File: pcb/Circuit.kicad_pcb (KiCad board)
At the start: 2 copper layers, 82.4 x 68.9 mm, 51 parts, among them J1 DTM13-12PA-R008, J2 TSW-101-07-T-D, J3 TSW-101-07-T-D, U1 MCP1700-1802E_TO92, U2 CDP68HC68S1, U3 LM2672N-5.0, U4 Teensy4.0, U5 MCP2562-H-P

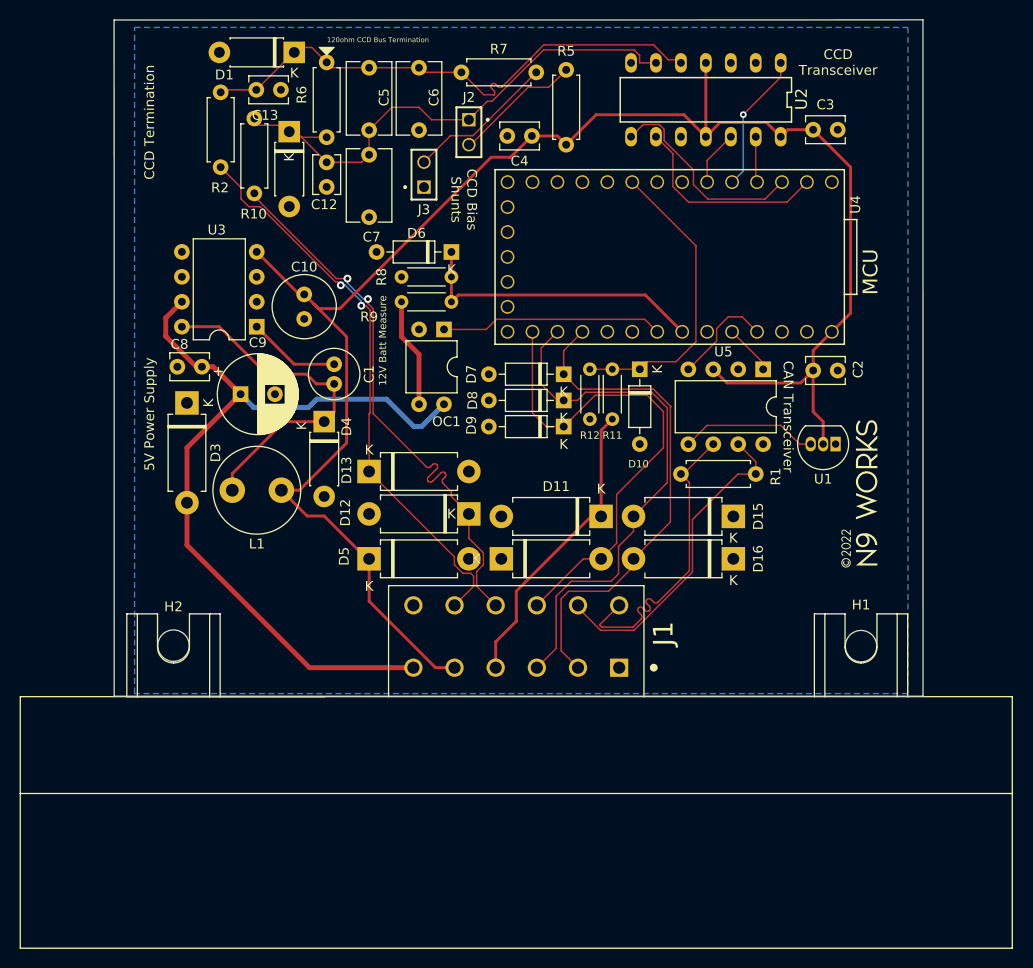
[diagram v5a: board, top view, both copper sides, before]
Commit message: Silkscreen tweaks
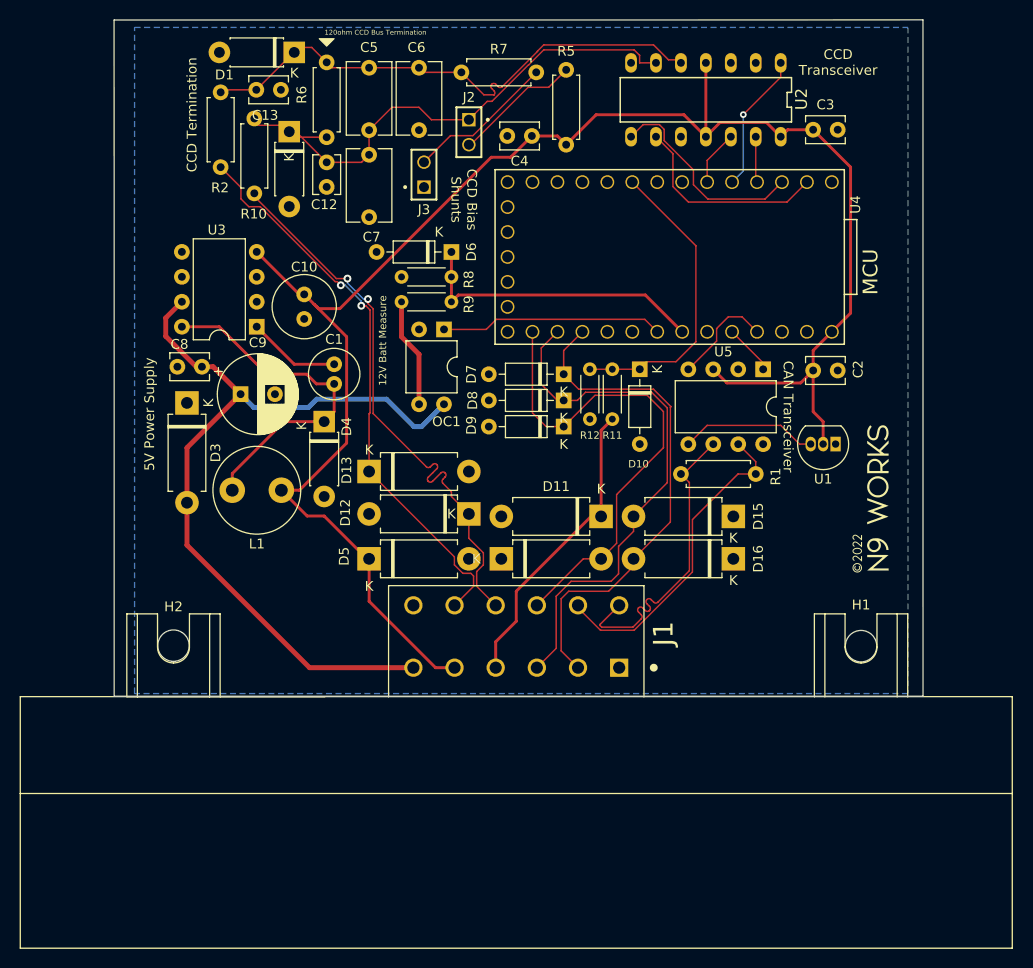
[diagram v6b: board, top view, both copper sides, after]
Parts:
- moved     1.25 mm to (127.3, 115.3)
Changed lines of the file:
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@@
     (property "Sheetname" "")
     (attr through_hole)
-    (fp_text reference "C5" (at 3.0085 -1.524 90) (layer "F.SilkS")
+    (fp_text reference "C5" (at -2.0715 0 180) (layer "F.SilkS")
       (effects (font (size 1 1) (thickness 0.15)))
     )
@@
     (property "Sheetname" "")
     (attr through_hole)
-    (fp_text reference "R9" (at 8.382 -1.524) (layer "F.SilkS")
+    (fp_text reference "R9" (at -1.778 -0.254 90) (layer "F.SilkS")
       (effects (font (size 1 1) (thickness 0.15)))
     )
@@
   )
   (footprint "Logos:N9Works" (layer "F.Cu")
-    (at 126.111 114.808 90)
+    (at 127.254 115.316 90)
     (attr board_only exclude_from_pos_files exclude_from_bom)
     (fp_text reference "   " (at 0 0 180) (layer "F.SilkS")
@@
     (property "Sheetname" "")
     (attr through_hole)
-    (fp_text reference "R8" (at 7.112 0 90) (layer "F.SilkS")
+    (fp_text reference "R8" (at -1.778 -0.254 90) (layer "F.SilkS")
       (effects (font (size 1 1) (thickness 0.15)))
     )
@@
     (property "Sheetname" "")
     (attr through_hole)
-    (fp_text reference "C1" (at 1.016 -3.556 -90) (layer "F.SilkS")
+    (fp_text reference "C1" (at -2.54 0) (layer "F.SilkS")
       (effects (font (size 1 1) (thickness 0.15)))
     )
@@
     (property "Sheetname" "")
     (attr through_hole)
-    (fp_text reference "C6" (at 3.0085 -1.524 -90) (layer "F.SilkS")
+    (fp_text reference "C6" (at -2.0715 0.254) (layer "F.SilkS")
       (effects (font (size 1 1) (thickness 0.15)))
     )
@@
     (property "Sheetname" "")
     (attr through_hole)
-    (fp_text reference "D6" (at 3.556 1.905 180) (layer "F.SilkS")
+    (fp_text reference "D6" (at -2.032 0 270) (layer "F.SilkS")
       (effects (font (size 1 1) (thickness 0.15)))
     )
@@
       (effects (font (size 1 1) (thickness 0.15)))
     )
-    (fp_text user "K" (at 0 -1.8 180) (layer "F.SilkS")
+    (fp_text user "K" (at 1.27 2.032 180) (layer "F.SilkS")
       (effects (font (size 1 1) (thickness 0.15)))
     )
@@
   (gr_poly
     (pts
-      (xy 71.882 70.104)
-      (xy 71.12 69.342)
-      (xy 72.644 69.342)
+      (xy 71.882 69.215)
+      (xy 71.12 68.453)
+      (xy 72.644 68.453)
     ) (layer "F.SilkS") (width 0.12) (fill solid))
   (gr_line (start 50.238 66.555) (end 132.588 66.541) (layer "Edge.Cuts") (width 0.05))
@@
     (effects (font (size 1.5 1.5) (thickness 0.3)))
   )
-  (gr_text "120ohm CCD Bus Termination" (at 82.296 68.58) (layer "F.SilkS")
+  (gr_text "120ohm CCD Bus Termination" (at 82.042 67.818) (layer "F.SilkS")
     (effects (font (size 0.5 0.5) (thickness 0.1)) (justify right))
   )
@@
     (effects (font (size 1 1) (thickness 0.2)))
   )
-  (gr_text "CCD Termination" (at 53.848 76.962 90) (layer "F.SilkS")
+  (gr_text "CCD Termination" (at 58.166 76.2 90) (layer "F.SilkS")
     (effects (font (size 1 1) (thickness 0.25)))
   )

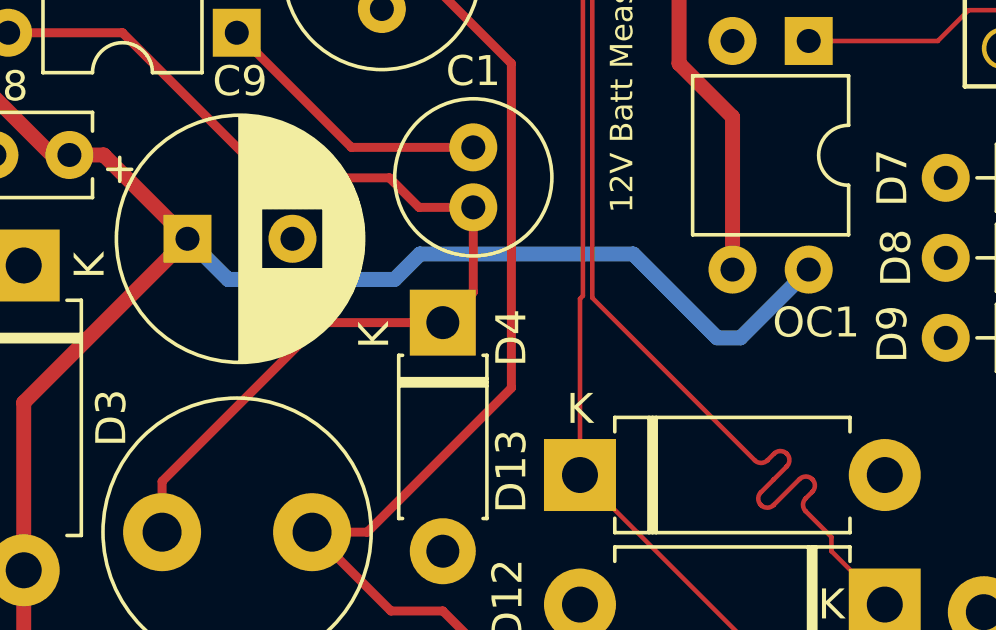
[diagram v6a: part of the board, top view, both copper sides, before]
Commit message: Undo attempt to simplify jumpers
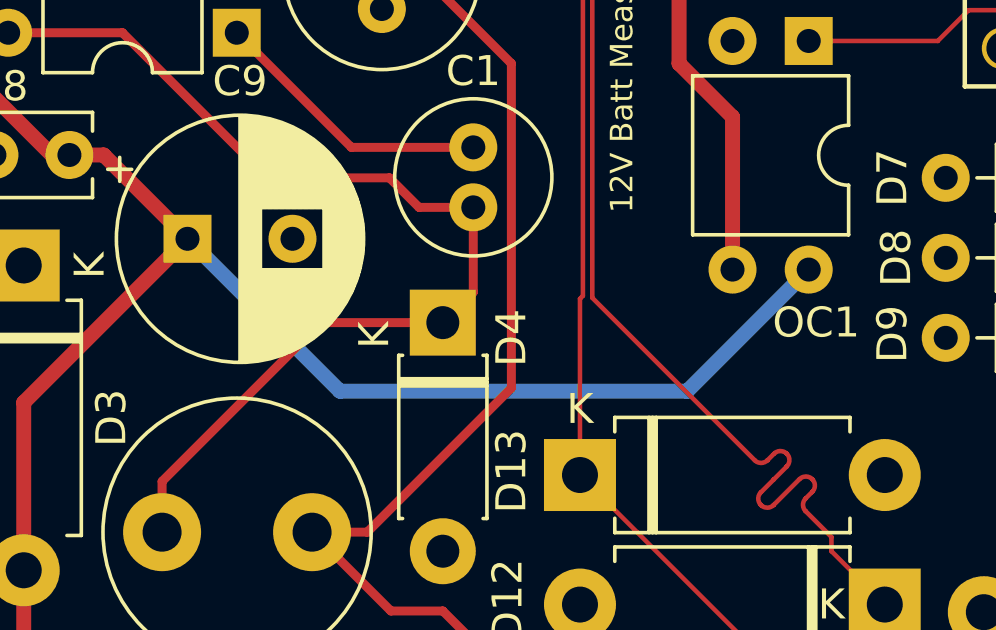
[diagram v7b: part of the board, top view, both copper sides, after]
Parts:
- R11: value 15K -> 10Kohm
- R12: value 10K -> 8Kohm
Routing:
- net +12V: track 83.8 -> 84.6 mm
